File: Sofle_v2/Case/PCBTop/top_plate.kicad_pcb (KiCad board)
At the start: 2 copper layers, 143.5 x 115.5 mm, 5 parts

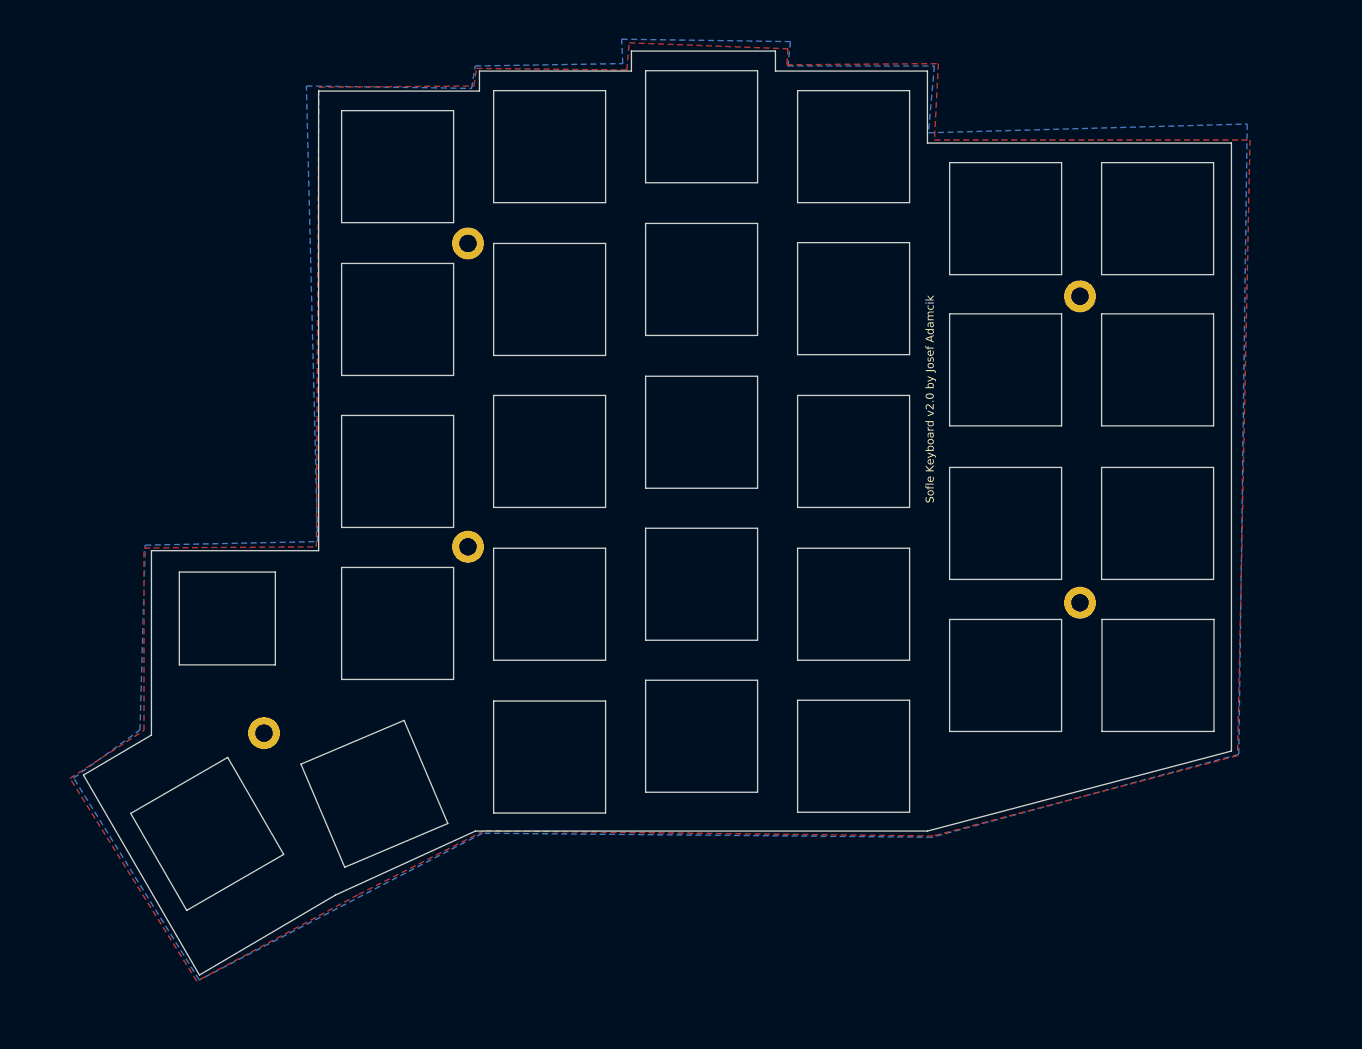
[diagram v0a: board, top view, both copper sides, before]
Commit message: Enlarge cutout for encoder in the top plate for versin 2
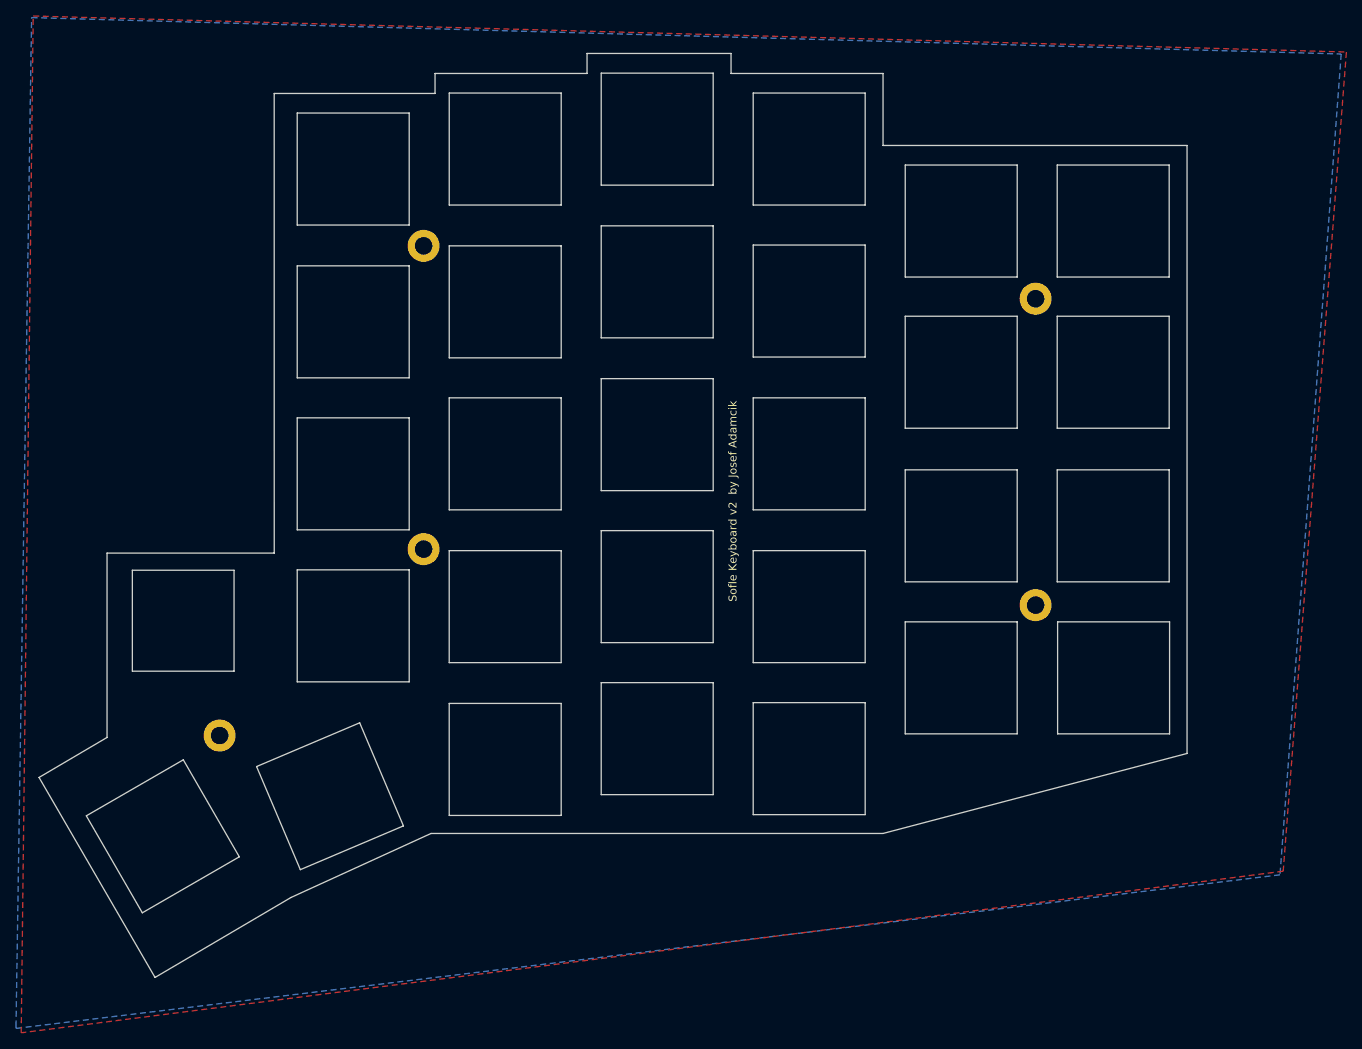
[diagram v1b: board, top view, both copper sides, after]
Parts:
- removed the ? at (72.3, 50.2)
- removed the ? at (148.8, 56.8)
- removed the ? at (148.8, 95.1)
- removed the ? at (46.8, 111.4)
- removed the ? at (72.3, 88.1)
- added ?: , Wire_Pads:SolderWirePad_single_0-8mmDrill, B.Cu at (66.7, 50.5)
- added ?: , Wire_Pads:SolderWirePad_single_0-8mmDrill, B.Cu at (143.2, 57.1)
- added ?: , Wire_Pads:SolderWirePad_single_0-8mmDrill, F.Cu at (143.2, 95.4)
- added ?: , Wire_Pads:SolderWirePad_single_0-8mmDrill, F.Cu at (41.2, 111.7)
- added ?: , Wire_Pads:SolderWirePad_single_0-8mmDrill, F.Cu at (66.7, 88.4)
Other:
- outline, holes or cut-outs redrawn
- board text added: "Sofle Keyboard v2 by Josef Adamcik"
- board text removed: "Sofle Keyboard v2.0 by Josef Adamcik"
